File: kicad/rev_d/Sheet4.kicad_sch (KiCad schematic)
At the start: 36 parts, among them J2 JUMPER, J3 JUMPER, X7 DB15VGA, X8 PLB1-4I, X9 PLB1-2

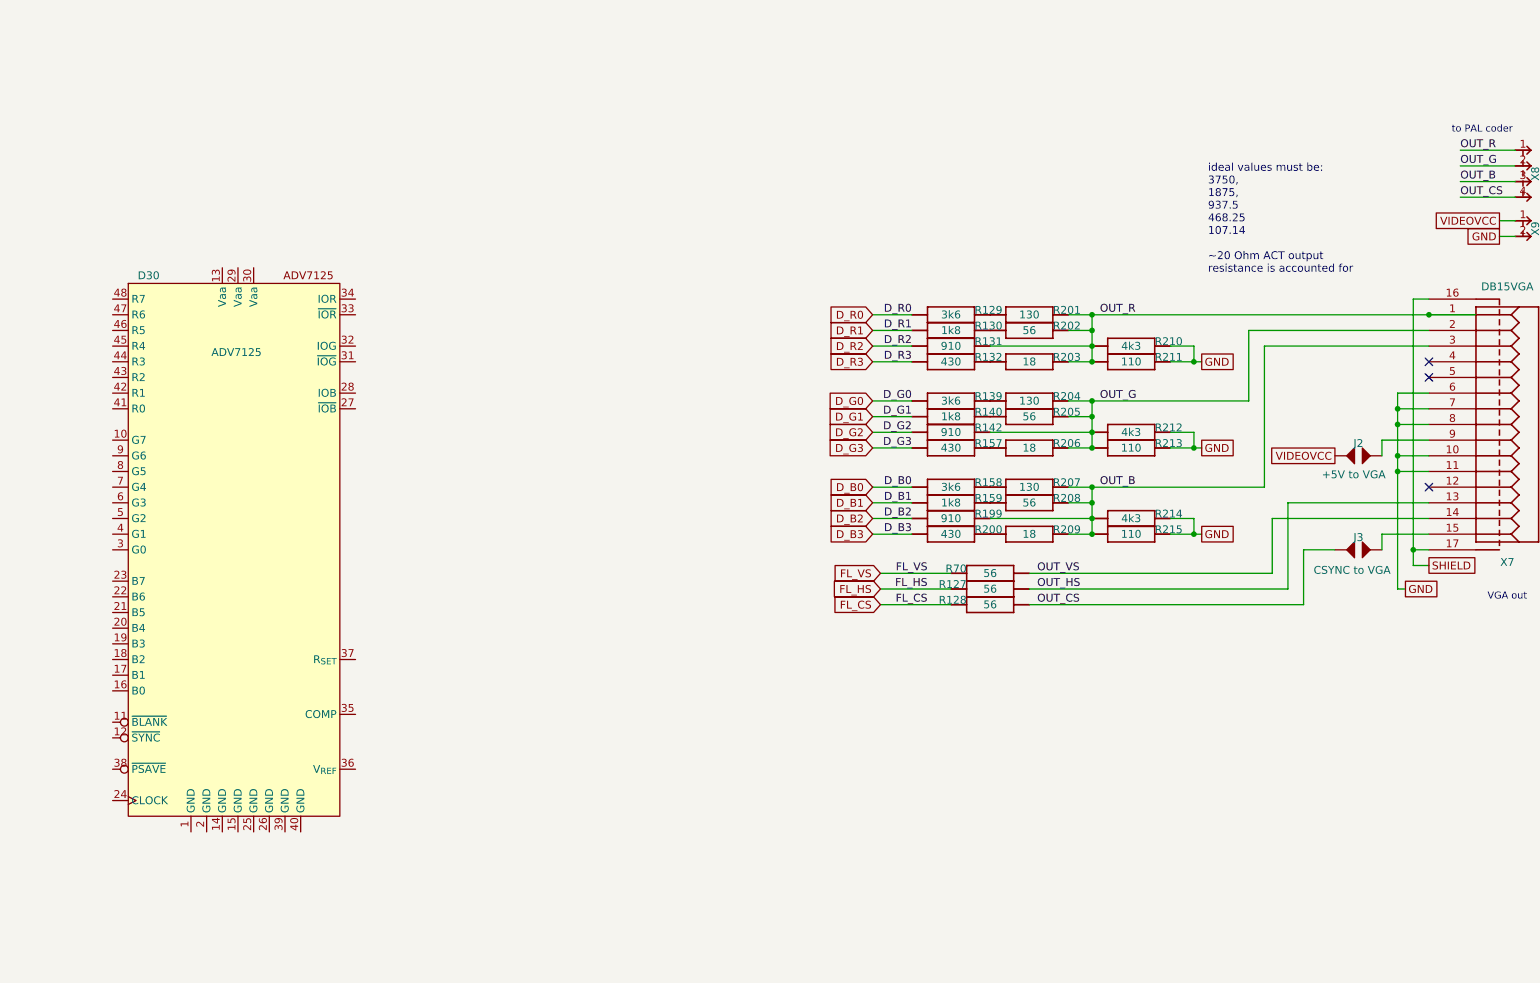
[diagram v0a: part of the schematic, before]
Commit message: pentevo: rev D: video output: use ADV7125 for analog video (WIP)
git-svn-id: svn://localhost/local-pentevo@1276 c6c76956-fad2-4150-a3a9-ea0a427205ba
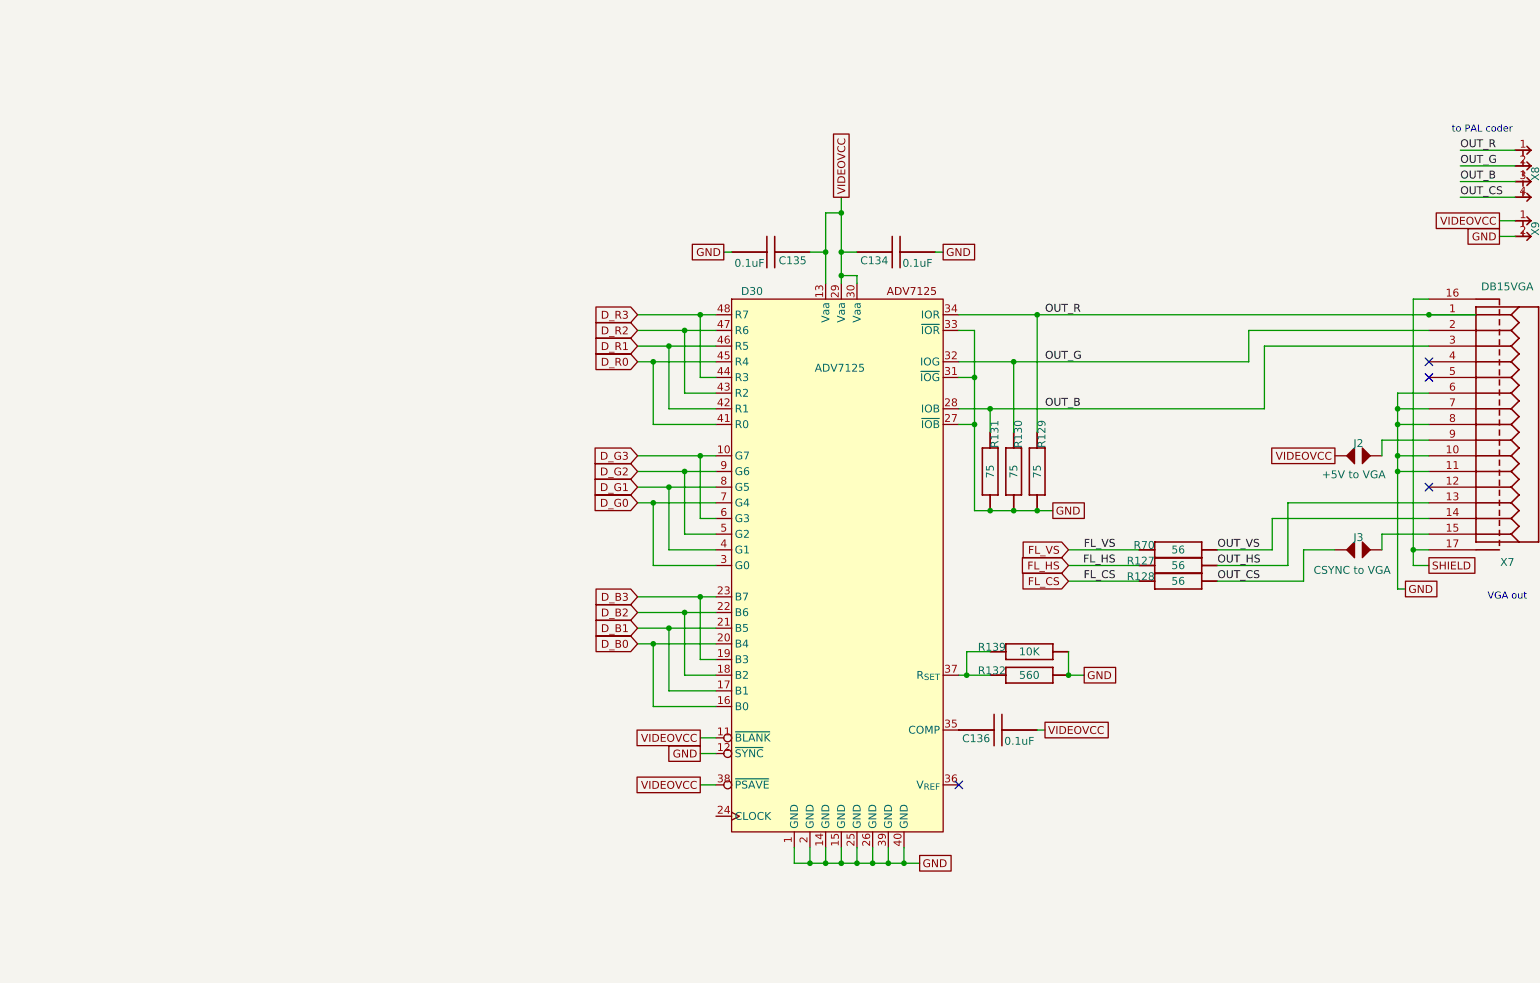
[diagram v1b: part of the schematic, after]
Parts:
- removed R129, R139, R158: 3k6, R-CHIP, symbol eva-altium-import:Sheet1_0_mirrored_RESCHIP
- removed R130, R140, R159: 1k8, R-CHIP, symbol eva-altium-import:Sheet1_0_mirrored_RESCHIP
- removed R131, R142, R199: 910, R-CHIP, symbol eva-altium-import:Sheet1_0_mirrored_RESCHIP
- removed R132, R157, R200: 430, R-CHIP, symbol eva-altium-import:Sheet1_0_mirrored_RESCHIP
- removed R201, R204, R207: 130, R-CHIP, symbol eva-altium-import:Sheet1_0_mirrored_RESCHIP
- removed R202, R205, R208: 56, R-CHIP, symbol eva-altium-import:Sheet1_0_mirrored_RESCHIP
- removed R203, R206, R209: 18, R-CHIP, symbol eva-altium-import:Sheet1_0_mirrored_RESCHIP
- removed R210, R212, R214: 4k3, R-CHIP, symbol eva-altium-import:Sheet1_0_mirrored_RESCHIP
- removed R211, R213, R215: 110, R-CHIP, symbol eva-altium-import:Sheet1_0_mirrored_RESCHIP
- added C134, C135, C136: 0.1uF, C-CHIP, symbol eva-altium-import:Sheet1_0_CAPCHIP
- added R129, R130, R131: 75, R-CHIP, symbol eva-altium-import:Sheet1_0_RESCHIP
- added R132: 560, R-CHIP, symbol eva-altium-import:Sheet1_0_RESCHIP
- added R139: 10K, R-CHIP, symbol eva-altium-import:Sheet1_0_RESCHIP
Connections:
- net D_B0: now also D30.16 (B0), D30.20 (B4)
- net D_B1: now also D30.17 (B1), D30.21 (B5)
- net D_B2: now also D30.18 (B2), D30.22 (B6)
- net D_B3: now also D30.19 (B3), D30.23 (B7)
- net D_G0: now also D30.3 (G0), D30.7 (G4)
- net D_G1: now also D30.4 (G1), D30.8 (G5)
- net D_G2: now also D30.5 (G2), D30.9 (G6)
- net D_G3: now also D30.10 (G7), D30.6 (G3)
- net D_R0: now also D30.41 (R0), D30.45 (R4)
- net D_R1: now also D30.42 (R1), D30.46 (R5)
- net D_R2: now also D30.43 (R2), D30.47 (R6)
- net D_R3: now also D30.44 (R3), D30.48 (R7)
- net GND: now also D30.1 (GND), D30.12 (~{SYNC}), D30.14 (GND), D30.15 (GND), D30.2 (GND), D30.25 (GND), D30.26 (GND), D30.27 (~{IOB}), D30.31 (~{IOG}), D30.33 (~{IOR}), D30.39 (GND), D30.40 (GND), C134.2, C135.2, R129.1 (i/o), R130.1 (i/o), R131.1 (i/o), R132.1 (i/o), R139.1 (i/o)
- net OUT_B: now also D30.28 (IOB), R131.2 (i/o1)
- net OUT_G: now also D30.32 (IOG), R130.2 (i/o1)
- net OUT_R: now also D30.34 (IOR), R129.2 (i/o1)
- net VIDEOVCC: now also D30.11 (~{BLANK}), D30.13 (Vaa), D30.29 (Vaa), D30.30 (Vaa), D30.38 (~{PSAVE}), C134.1, C135.1, C136.2
- net at D30.35 (COMP): now also C136.1
- net at D30.37 (R_{SET}): now also R132.2 (i/o1), R139.2 (i/o1)
- no-connect marks 3 -> 4
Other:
- note removed: "ideal values must be: 3750, 1875, 937.5 468.25 107.14 ~20 Ohm ACT output resistance is accounted for"
- moved on the sheet: D30, R127, R128, R70

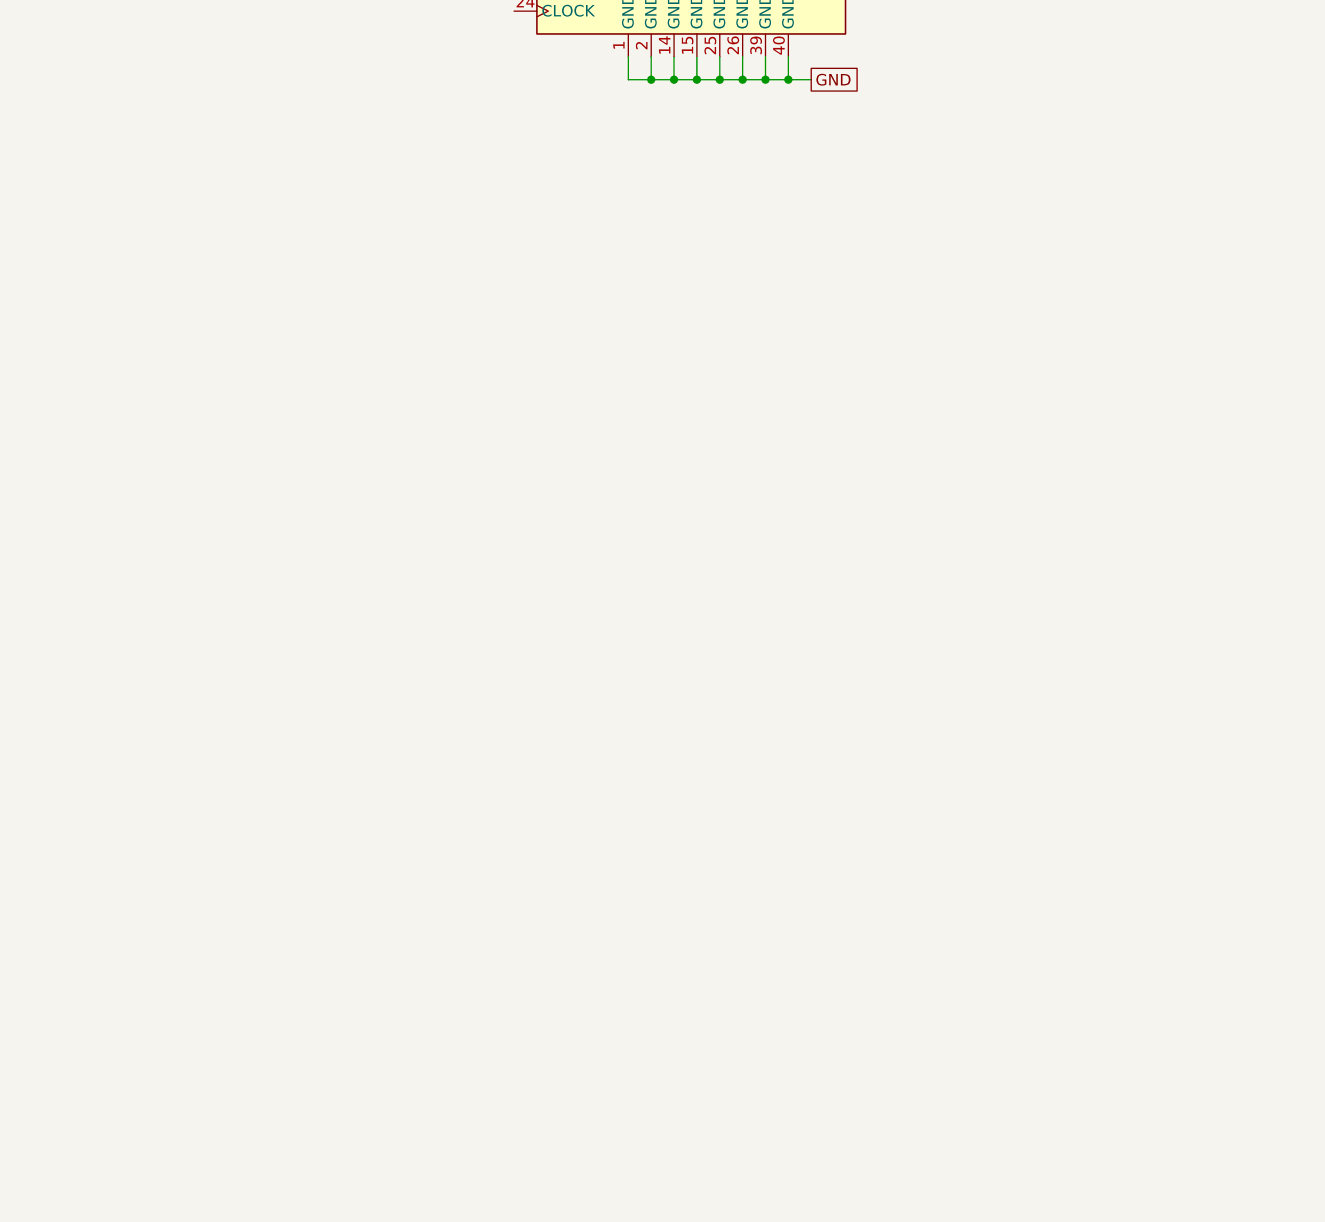
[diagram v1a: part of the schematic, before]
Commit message: pentevo: rev D: video output: add EPM3032 for de-DDRing video data and clock buffering
git-svn-id: svn://localhost/local-pentevo@1280 c6c76956-fad2-4150-a3a9-ea0a427205ba
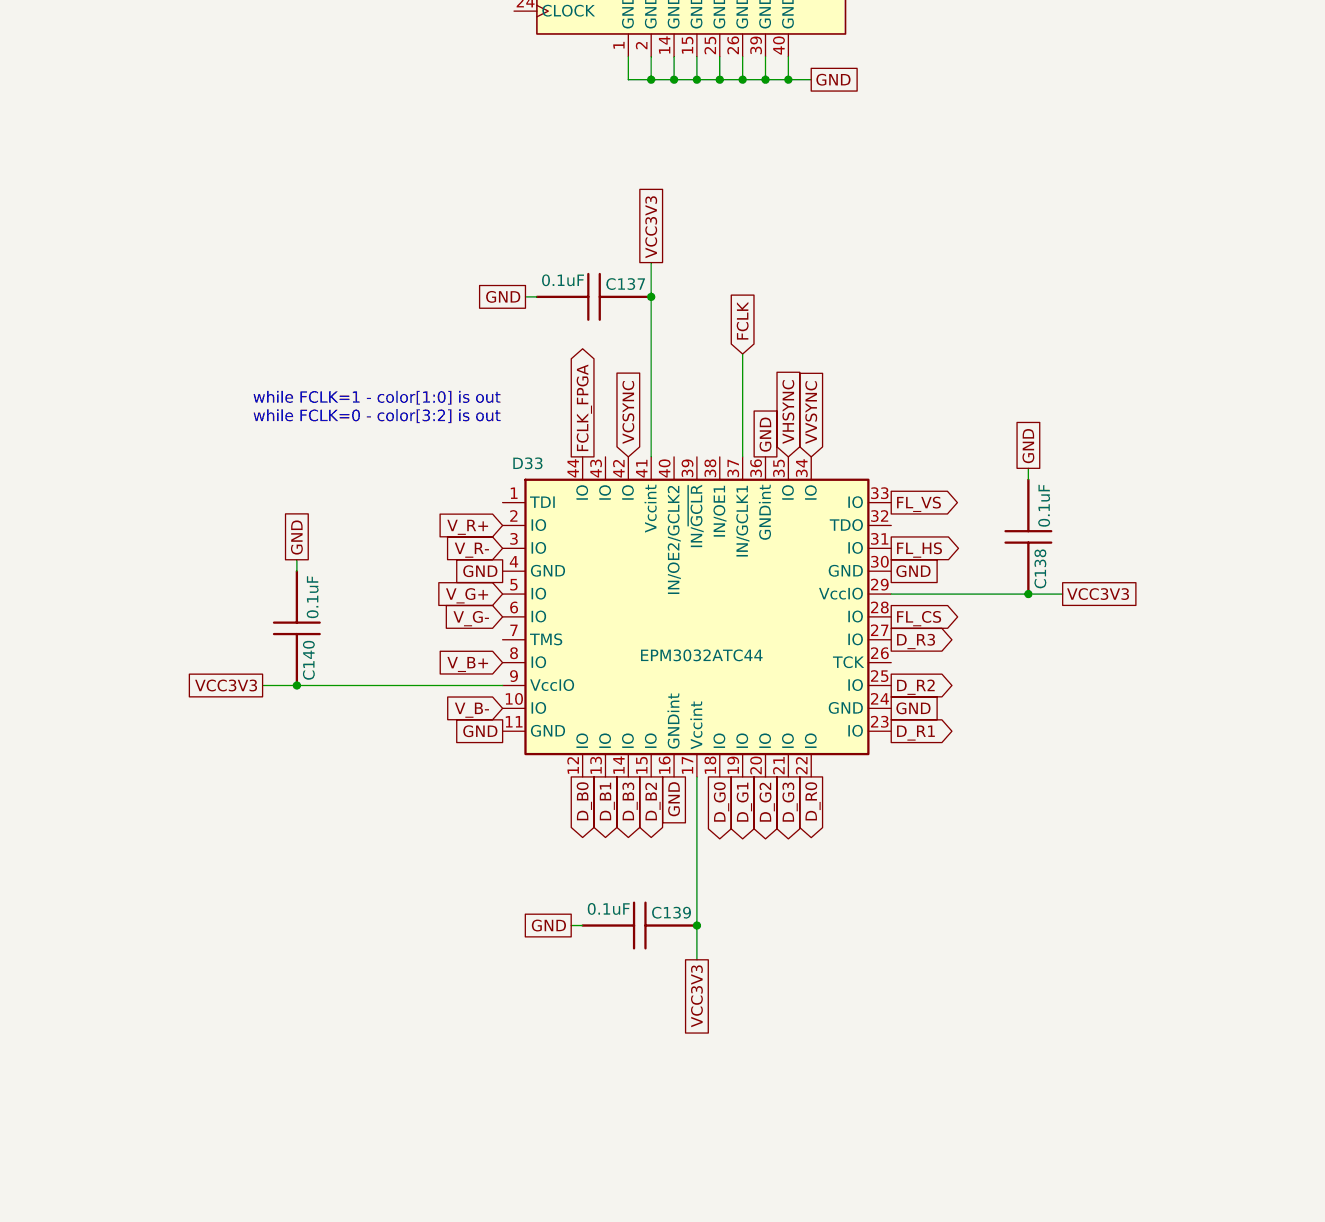
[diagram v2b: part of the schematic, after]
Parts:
- added C137, C138, C139, C140: 0.1uF, C-CHIP, symbol eva-altium-import:Sheet1_0_CAPCHIP
- added D33: EPM3032ATC44, symbol eva-altium-import:EPM3032ATC44
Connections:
- net D_B0: now also D33.12 (IO)
- net D_B1: now also D33.13 (IO)
- net D_B2: now also D33.15 (IO)
- net D_B3: now also D33.14 (IO)
- net D_G0: now also D33.18 (IO)
- net D_G1: now also D33.19 (IO)
- net D_G2: now also D33.20 (IO)
- net D_G3: now also D33.21 (IO)
- net D_R0: now also D33.22 (IO)
- net D_R1: now also D33.23 (IO)
- net D_R2: now also D33.25 (IO)
- net D_R3: now also D33.27 (IO)
- net FL_CS: now also D33.28 (IO)
- net FL_HS: now also D33.31 (IO)
- net FL_VS: now also D33.33 (IO)
- net GND: now also C137.2, C138.2, C139.2, C140.2, D33.11 (GND), D33.16 (GNDint), D33.24 (GND), D33.30 (GND), D33.36 (GNDint), D33.4 (GND)
- new net FCLK: D33.37 (IN/GCLK1)
- new net FCLK_FPGA: D33.44 (IO)
- new net VCC3V3: C137.1, C138.1, C139.1, C140.1, D33.17 (Vccint), D33.29 (VccIO), D33.41 (Vccint), D33.9 (VccIO)
- new net VCSYNC: D33.42 (IO)
- new net VHSYNC: D33.35 (IO)
- new net VVSYNC: D33.34 (IO)
- new net V_B+: D33.8 (IO)
- new net V_B-: D33.10 (IO)
- new net V_G+: D33.5 (IO)
- new net V_G-: D33.6 (IO)
- new net V_R+: D33.2 (IO)
- new net V_R-: D33.3 (IO)
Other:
- note added: "while FCLK=1 - color[1:0] is out while FCLK=0 - color[3:2] is out"
